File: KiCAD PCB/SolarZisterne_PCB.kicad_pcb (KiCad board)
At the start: 2 copper layers, 26 parts, among them J1 Erzeugung, J2 Verbrauch, J3 Solar, J4 Akku, J5 Ultraschall Sensor, J6 Externer Temperatur Sensor, J7 Interner Temperatur Sensor, J8 Erweiterung, U1 MCP1700T-3302E/MB, U2 MCP73871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

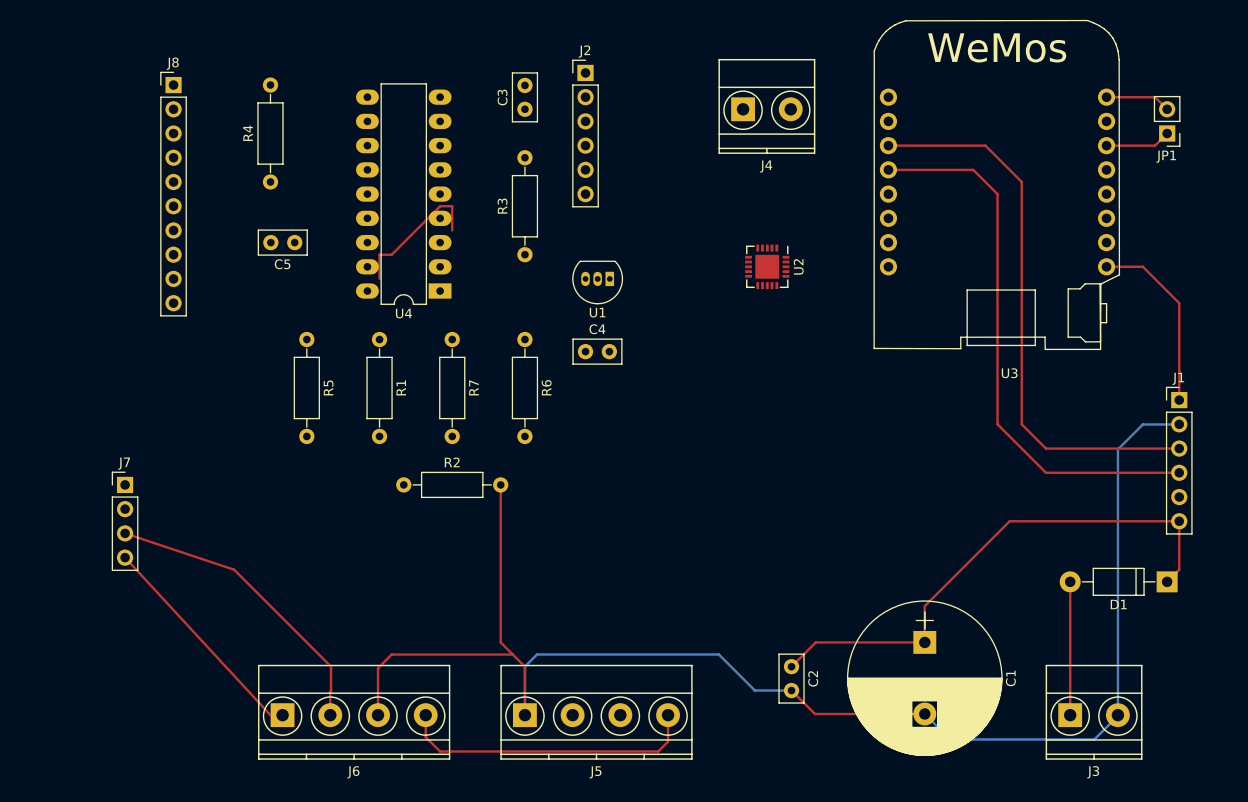
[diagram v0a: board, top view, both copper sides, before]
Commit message: Sicherung bevor die Messung mit den DHT22 Sensoren entfernt wird
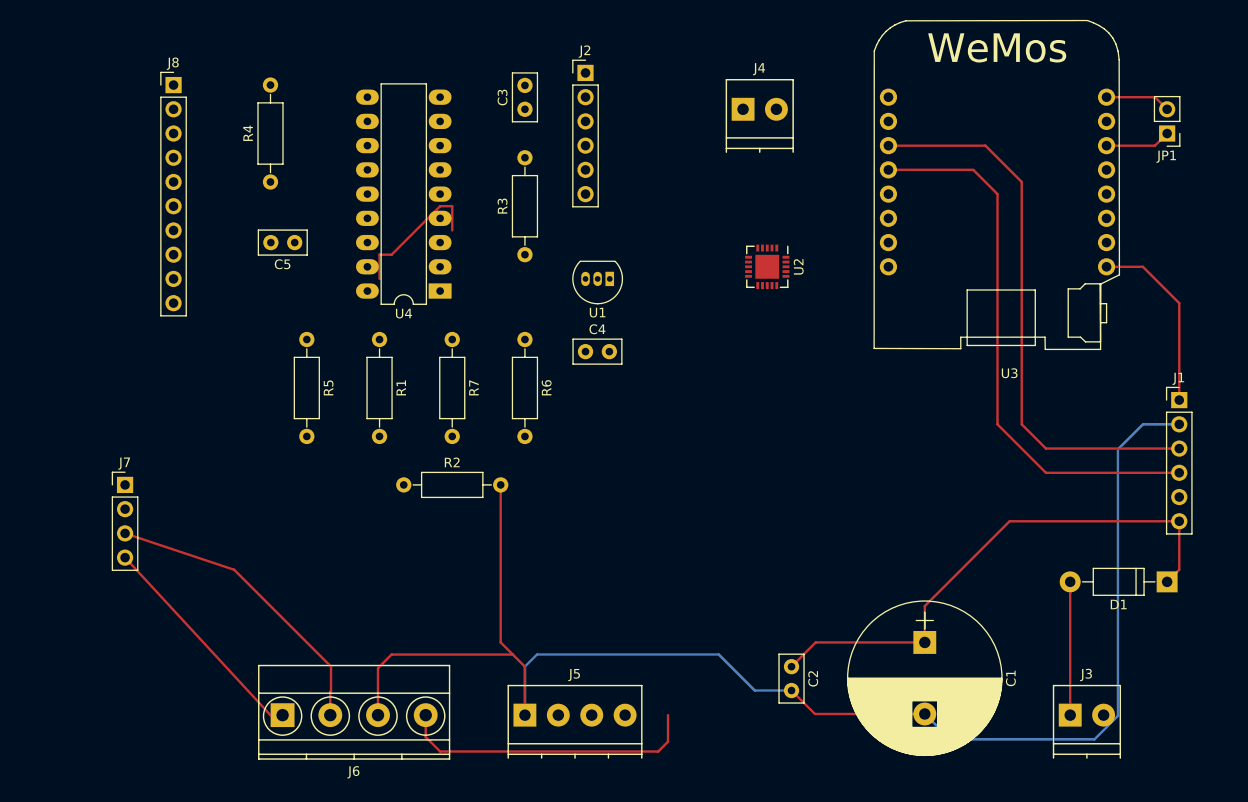
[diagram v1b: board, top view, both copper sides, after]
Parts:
- J3, J4: footprint Connectors_Terminal_Blocks:TerminalBlock_Pheonix_MKDS1.5-2pol -> Connectors_Terminal_Blocks:TerminalBlock_Pheonix_PT-3.5mm_2pol
- J5: footprint Connectors_Terminal_Blocks:TerminalBlock_Pheonix_MKDS1.5-4pol -> Connectors_Terminal_Blocks:TerminalBlock_Pheonix_PT-3.5mm_4pol
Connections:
- U3 pad 1: Net-(U3-Pad1) -> (no net)
- U3 pad 12: Net-(U3-Pad12) -> (no net)
- U3 pad 13: Net-(U3-Pad13) -> (no net)
- U3 pad 14: Net-(U3-Pad14) -> (no net)
- U3 pad 15: Net-(U3-Pad15) -> (no net)
- U3 pad 7: Net-(U3-Pad7) -> (no net)
- U3 pad 8: Net-(U3-Pad8) -> (no net)
- U4 pad 8: Net-(U4-Pad8) -> (no net)

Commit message: PCB Update
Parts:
- added J10: GS2, Connectors:GS2, F.Cu at (92.7, 49.5)
- added J11: GS2, Connectors:GS2, F.Cu at (92.7, 57.1)
- added J12: GS2, Connectors:GS2, F.Cu at (92.7, 63.5)
- added J13: GS2, Connectors:GS2, F.Cu at (92.7, 68.6)
- added J9: GS2, Connectors:GS2, F.Cu at (92.7, 43.2)
- J6: footprint Connectors_Terminal_Blocks:TerminalBlock_Pheonix_MKDS1.5-4pol -> Connectors_Terminal_Blocks:TerminalBlock_Pheonix_PT-3.5mm_4pol
- J7: footprint Pin_Headers:Pin_Header_Straight_1x04_Pitch2.54mm -> Pin_Headers:Pin_Header_Straight_1x06_Pitch2.54mm
- moved J4 68.5 mm to (145.3, 109.2)
- moved J6 59.4 mm to (178.8, 109.2)
- moved J7 26.4 mm to (124.5, 99.1)
- moved D1 26.2 mm to (186.1, 90.8), turned to 270 degrees
- moved C2 25.1 mm to (150.4, 91.4)
- moved C1 21.3 mm to (169.5, 87.6)
- moved J1 17.8 mm to (197.1, 82.3)
- moved J5 13.3 mm to (158.0, 109.2)
- moved U2 12.7 mm to (169.5, 73.7)
- moved U3 3.81 mm to (198.1, 53.3)
- moved JP1 3.24 mm to (215.3, 47.6)
- moved J3 2.29 mm to (200.0, 109.2)
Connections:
- U3 pad 3: /Echo -> /SCL
- U3 pad 4: /Trig -> /SDA
- U3 pad 5: /SDA -> /Trig
- U3 pad 6: /SCL -> /Echo
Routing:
- net /SCL: track 90.0 -> 0.00 mm
- net /SDA: track 81.5 -> 0.00 mm
- net GND: track 152.8 -> 102.0 mm
- net Net-(C1-Pad1): track 56.1 -> 30.6 mm
- net (no net): track 14.8 -> 0.00 mm
- net +3V3: track 50.9 -> 43.6 mm
- net Net-(D1-Pad2): track 14.0 -> 16.2 mm
- net Net-(JP1-Pad1): track 6.88 -> 5.76 mm
- net Net-(JP1-Pad2): track 6.88 -> 6.11 mm
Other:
- board outline added: 99.1 x 74.3 mm

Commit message: PCB update
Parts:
- removed C3: 4.7uF, Capacitors_THT:C_Disc_D5.0mm_W2.5mm_P2.50mm
- removed C4: 1uF, Capacitors_THT:C_Disc_D5.0mm_W2.5mm_P2.50mm
- removed U1: MCP1700T-3302E/MB, TO_SOT_Packages_THT:TO-92_Inline_Narrow_Oval
- added J14: Buck-Conv D24V5F3, Pin_Headers:Pin_Header_Straight_1x04_Pitch2.54mm, F.Cu at (152.7, 100.3)
- J10, J11, J12, J13, J9, U2: moved to B.Cu
- moved J5 66.2 mm to (179.8, 46.7), turned to 180 degrees
- moved C5 61.3 mm to (162.6, 103.1)
- moved R4 59.6 mm to (160.5, 94.0), turned to 0 degrees
- moved R5 48.9 mm to (160.5, 98.6), turned to 0 degrees
- moved J9 48.4 mm to (136.1, 64.5), turned to 270 degrees
- moved J10 48.3 mm to (136.1, 70.6), turned to 270 degrees
- moved J11 47.4 mm to (136.1, 76.2), turned to 270 degrees
- moved J13 47.3 mm to (136.1, 87.4), turned to 270 degrees
- moved J12 47.1 mm to (136.1, 81.8), turned to 270 degrees
- moved J2 45.8 mm to (152.9, 86.4), turned to 180 degrees
- moved U4 45.6 mm to (179.8, 75.7)
- moved R2 41.6 mm to (149.9, 46.2), turned to 270 degrees
- moved R1 30.5 mm to (157.5, 56.4), turned to 90 degrees
- moved J8 29.2 mm to (127.0, 64.0)
- moved R7 22.6 mm to (133.6, 46.2)
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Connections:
- J4 pad 1: GND -> Net-(C5-Pad1)
- J4 pad 2: Net-(C5-Pad1) -> GND
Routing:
- net +3V3: track 43.6 -> 213.1 mm
- net GND: track 102.0 -> 218.5 mm
- net /SCL: track 0.00 -> 78.5 mm, vias 0 -> 1
- net /SDA: track 0.00 -> 71.7 mm
- net Net-(C5-Pad1): track 0.00 -> 43.2 mm
- net Net-(J14-Pad3): track 0.00 -> 35.1 mm
- net Net-(C1-Pad1): track 30.6 -> 51.3 mm
- net /Trig: track 0.00 -> 16.8 mm
- net Net-(J2-Pad6): track 0.00 -> 14.0 mm
- net /Echo: track 0.00 -> 12.5 mm
- net Net-(D1-Pad2): track 16.2 -> 8.13 mm
- net (no net): track 0.00 -> 3.00 mm
- net Net-(JP1-Pad2): track 6.11 -> 7.74 mm
- net /PG: track 0.00 -> 1.02 mm
- net Net-(JP1-Pad1): track 5.76 -> 6.68 mm

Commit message: fast aller Leiterbahnen
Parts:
- U3: value WeMos_mini -> WeMos_Mini
- moved R7 25.4 mm to (157.5, 54.9), turned to 180 degrees
- moved R1 18.8 mm to (157.5, 75.2)
- moved R6 16.0 mm to (157.5, 49.3), turned to 180 degrees
- moved R2 15.7 mm to (157.5, 59.9), turned to 180 degrees
- moved C5 5.68 mm to (160.0, 108.2), turned to 270 degrees
- moved JP1 2.54 mm to (215.4, 47.8)
- moved C1 2.09 mm to (181.4, 85.9)
- moved J3 2.03 mm to (187.5, 109.2)
- moved R5 2.03 mm to (160.5, 100.6)
- moved D1 1.83 mm to (178.3, 100.6)
- moved J4 1.52 mm to (166.1, 109.2)
- moved R3 1.52 mm to (165.1, 56.9)
- moved J1 1.52 mm to (197.1, 83.8)
- moved U3 0.72 mm to (198.6, 53.8)
- moved C2 0.51 mm to (167.1, 86.4)
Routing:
- net GND: track 218.5 -> 336.1 mm
- net /SDA: track 71.7 -> 188.4 mm, vias 0 -> 1
- net /Analog1: track 0.00 -> 111.7 mm
- net /SCL: track 78.5 -> 185.2 mm, vias 1 -> 2
- net /GPB3: track 0.00 -> 53.0 mm, vias 0 -> 1
- net VCC: track 0.00 -> 44.8 mm
- net Net-(R5-Pad1): track 0.00 -> 26.9 mm
- net /PG: track 1.02 -> 24.9 mm
- net /STAT2: track 0.00 -> 21.9 mm
- net /STAT1: track 0.00 -> 20.1 mm
- net Net-(R4-Pad1): track 0.00 -> 18.1 mm
- net /Trig: track 16.8 -> 34.0 mm
- net Net-(R1-Pad2): track 0.00 -> 16.9 mm
- net Net-(R3-Pad1): track 0.00 -> 14.0 mm
- net /GPB4: track 0.00 -> 11.0 mm
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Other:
- board size 99.1 x 74.3 mm -> 95.5 x 74.3 mm
